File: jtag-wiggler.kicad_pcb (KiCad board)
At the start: 2 copper layers, 152.4 x 101.6 mm, 50 parts, among them J1 DSUB-25_Male_Horizontal_P2.77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, J2 BarrelJack_Horizontal, P1 PinHeader_1x02_P2.54mm_Vertic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, P2 PinHeader_1x03_P2.54mm_Vertic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, P3 PinHeader_1x08_P2.54mm_Vertic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, Q1 TO-92_Wide, SW1 SW_Generic, U1 DIP-20_W7.62mm_Socket_LongPads, U2 TO-220-3_Vertical, U3 TO-220-3_Vertical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

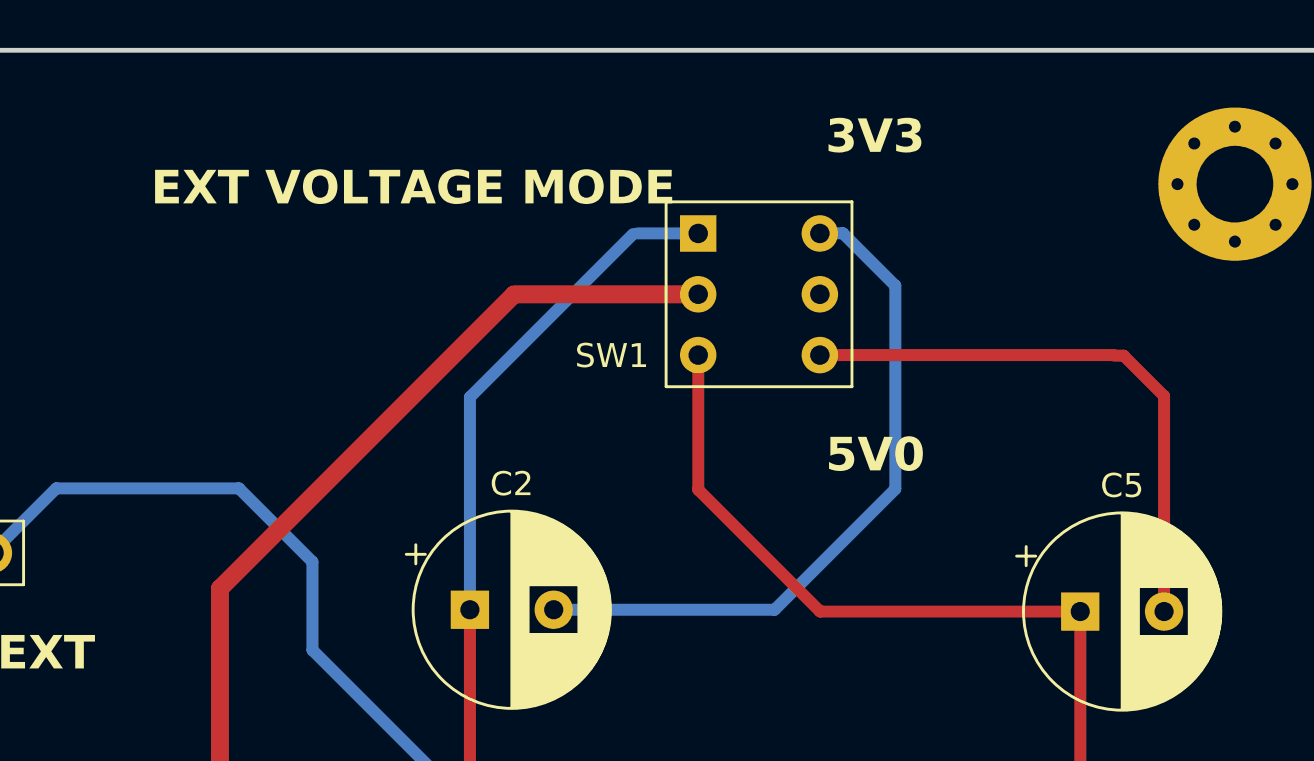
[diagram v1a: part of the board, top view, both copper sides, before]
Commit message: Update SW1 footprint; fits up to 1.5mm pin width
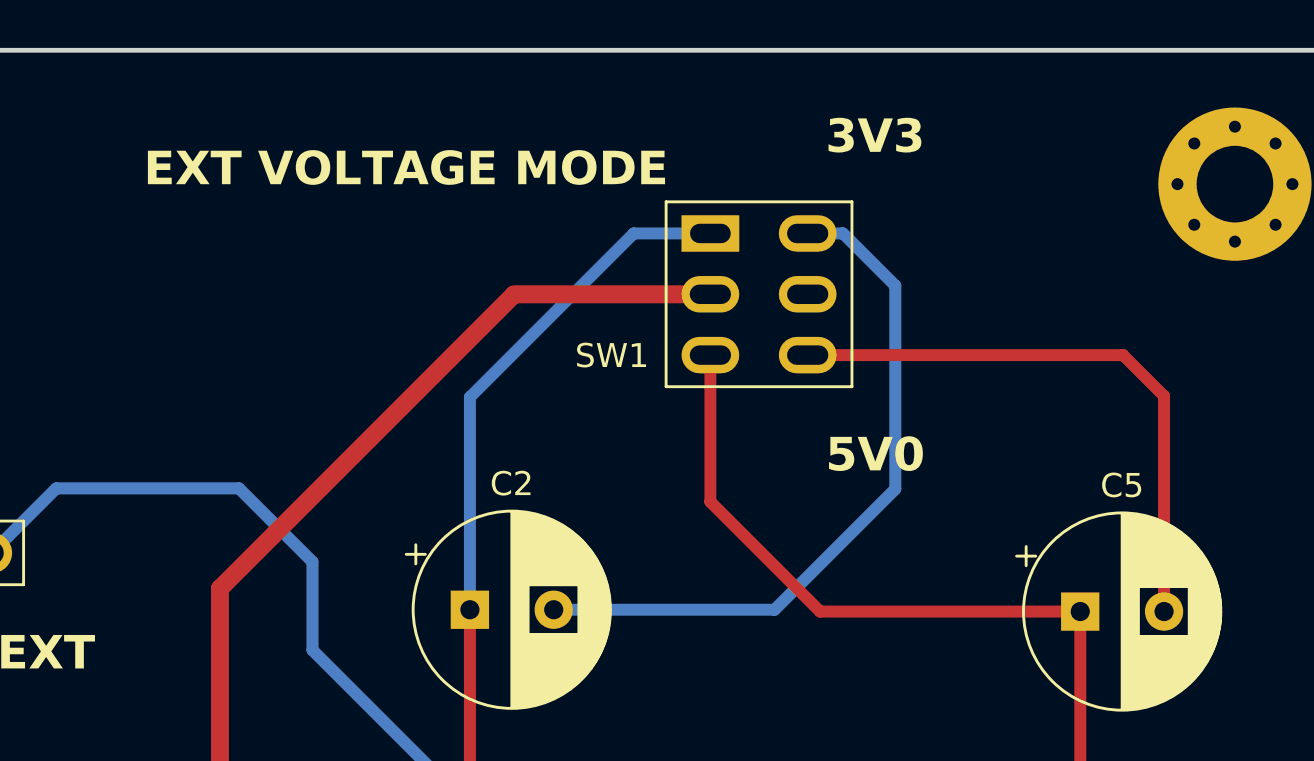
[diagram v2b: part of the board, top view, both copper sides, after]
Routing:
- net C2_positive: track 45.2 -> 45.9 mm
- net C2_negative: track 28.9 -> 29.4 mm
- net C5_negative: track 24.1 -> 24.6 mm
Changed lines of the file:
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@@
     (fp_line (start 6.31 6.29) (end 6.31 -1.21)
       (stroke (width 0.1) (type solid)) (layer "F.Fab"))
-    (pad "1" thru_hole rect (at 0 0) (size 1.524 1.524) (drill 0.8128) (layers "*.Cu" "*.Mask")
+    (pad "1" thru_hole rect (at 0.508 0) (size 2.413 1.524) (drill oval 1.7024 0.8128) (layers "*.Cu" "*.Mask")
       (net 10 "C2_positive"))
-    (pad "2" thru_hole circle (at 0 2.54) (size 1.524 1.524) (drill 0.8128) (layers "*.Cu" "*.Mask")
+    (pad "2" thru_hole oval (at 0.508 2.54) (size 2.413 1.524) (drill oval 1.724 0.8128) (layers "*.Cu" "*.Mask")
       (net 1 "Protected_VCC"))
-    (pad "3" thru_hole circle (at 0 5.08) (size 1.524 1.524) (drill 0.8128) (layers "*.Cu" "*.Mask")
+    (pad "3" thru_hole oval (at 0.508 5.08) (size 2.413 1.524) (drill oval 1.724 0.8128) (layers "*.Cu" "*.Mask")
       (net 24 "C5_positive"))
-    (pad "4" thru_hole circle (at 5.08 5.08) (size 1.524 1.524) (drill 0.8128) (layers "*.Cu" "*.Mask")
+    (pad "4" thru_hole oval (at 4.572 5.08) (size 2.413 1.524) (drill oval 1.724 0.8128) (layers "*.Cu" "*.Mask")
       (net 26 "C5_negative"))
-    (pad "5" thru_hole circle (at 5.08 2.54) (size 1.524 1.524) (drill 0.8128) (layers "*.Cu" "*.Mask")
+    (pad "5" thru_hole oval (at 4.572 2.54) (size 2.413 1.524) (drill oval 1.724 0.8128) (layers "*.Cu" "*.Mask")
       (net 3 "GND"))
-    (pad "6" thru_hole circle (at 5.08 0) (size 1.524 1.524) (drill 0.8128) (layers "*.Cu" "*.Mask")
+    (pad "6" thru_hole oval (at 4.572 0) (size 2.413 1.524) (drill oval 1.724 0.8128) (layers "*.Cu" "*.Mask")
       (net 25 "C2_negative"))
     (model "${KICAD6_3DMODEL_DIR}/Button_Switch_THT.3dshapes/SW_NKK_G1xJP.wrl"
@@
     (effects (font (size 1.4 1.4) (thickness 0.28) bold) (justify left bottom))
   )
-  (gr_text "EXT VOLTAGE MODE" (at 175.325 54.825) (layer "F.SilkS")
+  (gr_text "EXT VOLTAGE MODE" (at 175.025 54.025) (layer "F.SilkS")
     (effects (font (size 1.4 1.4) (thickness 0.28) bold) (justify left bottom))
   )
@@
   (segment (start 194.8 93.275) (end 194.8 88.6) (width 0.5) (layer "F.Cu") (net 10))
   (segment (start 188.65 82.45) (end 188.65 71.625) (width 0.5) (layer "F.Cu") (net 10))
-  (segment (start 198.185 55.91) (end 195.65 55.91) (width 0.5) (layer "B.Cu") (net 10))
-  (segment (start 188.65 62.75) (end 188.65 71.625) (width 0.5) (layer "B.Cu") (net 10))
-  (segment (start 195.465 55.935) (end 188.65 62.75) (width 0.5) (layer "B.Cu") (net 10))
+  (segment (start 188.65 62.75) (end 195.49 55.91) (width 0.5) (layer "B.Cu") (net 10))
+  (segment (start 188.65 71.625) (end 188.65 62.75) (width 0.5) (layer "B.Cu") (net 10))
+  (segment (start 195.49 55.91) (end 198.693 55.91) (width 0.5) (layer "B.Cu") (net 10))
   (segment (start 159.775 98.875) (end 159.795 98.895) (width 0.5) (layer "F.Cu") (net 11))
   (segment (start 132.55 71.65) (end 132.55 62.05) (width 0.5) (layer "F.Cu") (net 11))
@@
   (segment (start 87.475 91.55) (end 86.425 90.5) (width 0.5) (layer "B.Cu") (net 23))
   (segment (start 86.425 90.5) (end 84.44 90.5) (width 0.5) (layer "B.Cu") (net 23))
-  (segment (start 198.185 60.99) (end 198.185 66.61) (width 0.5) (layer "F.Cu") (net 24))
-  (segment (start 203.275 71.7) (end 214.140056 71.7) (width 0.5) (layer "F.Cu") (net 24))
   (segment (start 214.140056 83.044944) (end 214.065 83.12) (width 0.5) (layer "F.Cu") (net 24))
+  (segment (start 198.693 60.99) (end 198.693 67.118) (width 0.5) (layer "F.Cu") (net 24))
   (segment (start 214.140056 83.075) (end 214.040056 83.175) (width 0.5) (layer "F.Cu") (net 24))
   (segment (start 214.140056 71.7) (end 214.140056 83.044944) (width 0.5) (layer "F.Cu") (net 24))
-  (segment (start 198.185 66.61) (end 203.275 71.7) (width 0.5) (layer "F.Cu") (net 24))
+  (segment (start 203.275 71.7) (end 214.140056 71.7) (width 0.5) (layer "F.Cu") (net 24))
+  (segment (start 198.693 67.118) (end 203.275 71.7) (width 0.5) (layer "F.Cu") (net 24))
   (segment (start 201.374999 71.625) (end 192.15 71.625) (width 0.5) (layer "B.Cu") (net 25))
-  (segment (start 203.265 55.91) (end 203.273853 55.901147) (width 0.5) (layer "B.Cu") (net 25))
-  (segment (start 203.273853 55.901147) (end 204.226146 55.901147) (width 0.5) (layer "B.Cu") (net 25))
+  (segment (start 202.757 55.91) (end 204.217293 55.91) (width 0.5) (layer "B.Cu") (net 25))
+  (segment (start 204.217293 55.91) (end 204.226146 55.901147) (width 0.25) (layer "B.Cu") (net 25))
   (segment (start 206.416147 58.091148) (end 206.416147 66.583852) (width 0.5) (layer "B.Cu") (net 25))
   (segment (start 204.226146 55.901147) (end 206.416147 58.091148) (width 0.5) (layer "B.Cu") (net 25))
   (segment (start 206.416147 66.583852) (end 201.374999 71.625) (width 0.5) (layer "B.Cu") (net 25))
-  (segment (start 215.575 61.015) (end 215.955 61.015) (width 0.5) (layer "F.Cu") (net 26))
-  (segment (start 215.55 60.99) (end 215.575 61.015) (width 0.25) (layer "F.Cu") (net 26))
-  (segment (start 203.265 60.99) (end 215.55 60.99) (width 0.5) (layer "F.Cu") (net 26))
-  (segment (start 215.955 61.015) (end 217.640056 62.700056) (width 0.5) (layer "F.Cu") (net 26))
-  (segment (start 217.640056 62.700056) (end 217.640056 71.7) (width 0.5) (layer "F.Cu") (net 26))
+  (segment (start 215.93 60.99) (end 202.757 60.99) (width 0.5) (layer "F.Cu") (net 26))
+  (segment (start 217.640056 71.7) (end 217.640056 62.700056) (width 0.5) (layer "F.Cu") (net 26))
+  (segment (start 217.640056 62.700056) (end 215.93 60.99) (width 0.5) (layer "F.Cu") (net 26))
   (segment (start 140.225 89.375) (end 140.17 89.32) (width 0.5) (layer "F.Cu") (net 29))
   (segment (start 140.17 89.32) (end 140.17 62.05) (width 0.5) (layer "F.Cu") (net 29))
